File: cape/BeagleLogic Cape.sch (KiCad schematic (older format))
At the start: 21 parts, among them P1 CONN_02X14, Q1 BSS138, U1 bbb, U2 74LVCH16245, U3 AT24CS64-SSHM

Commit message: update schema, pcb to kicad5 libs
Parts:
- removed P1: CONN_02X14, Pin_Headers:Pin_Header_Angled_2x14, symbol CONN_02X14
- removed Q1: BSS138, SMD_Packages:SOT-23, symbol BSS138
- removed U3: AT24CS64-SSHM, SMD_Packages:SOIC-8-W, symbol AT24CS64-SSHM
- added J101: Conn_02x14_Odd_Even, Pin_Headers:Pin_Header_Angled_2x14, symbol Connector_Generic:Conn_02x14_Odd_Even
- added Q101: BSS138, Housings_SOT-23_SOT-143_TSOT-6:SOT-23_Handsoldering, symbol Transistor_FET:BSS138
- added U101: AT24CS64-SSHM, SMD_Packages:SOIC-8-N, symbol Memory_EEPROM:AT24CS64-SSHM
- C1, C2: symbol C -> pspice:C
- R1, R10, R12, R13, R14, R15, R2, R3, R4, R5, R6, R7, R8, R9: symbol R -> pspice:R
- U1: symbol bbb -> bbb:bbb
- U2: symbol 74LVCH16245 -> 74LVCH16245:74LVCH16245
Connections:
- wire segments 151 -> 199
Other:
- moved on the sheet: C1, C2, R1, R10, R12, R13, R14, R15, R2, R3, R4, R5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

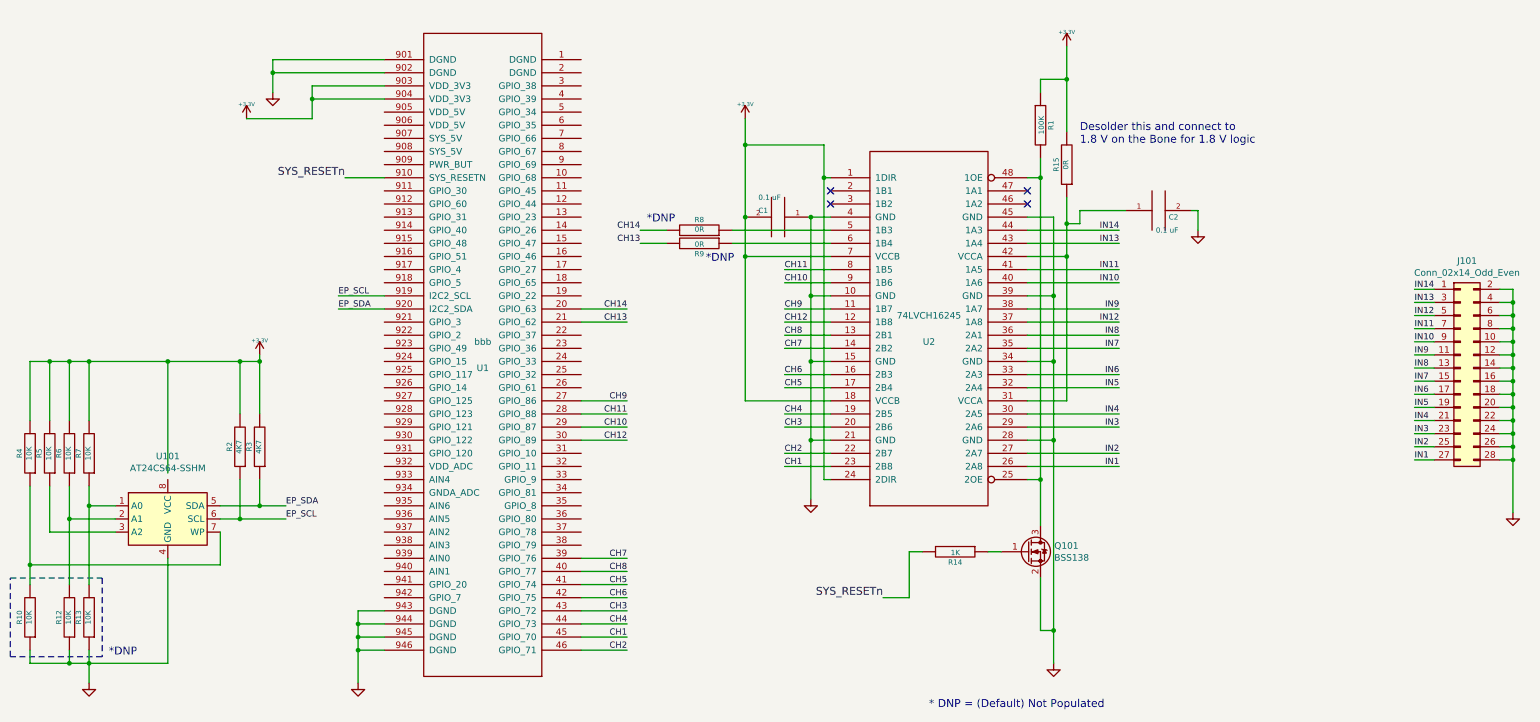
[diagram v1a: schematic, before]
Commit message: make the cape pass electrical rules check
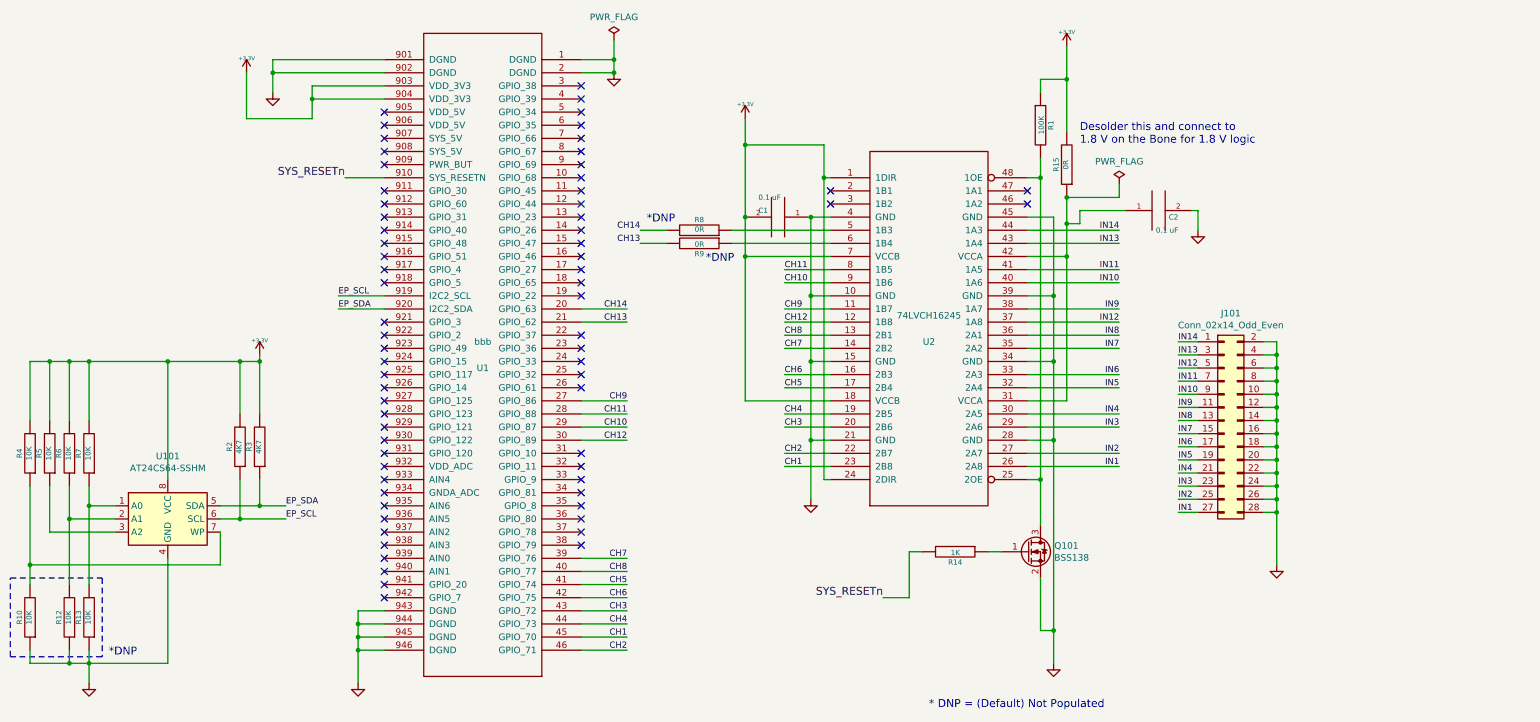
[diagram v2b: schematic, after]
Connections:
- net +3V3: now also U101.8 (VCC)
- net GND: now also U1.1 (DGND), U1.2 (DGND)
- no-connect marks 4 -> 69
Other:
- moved on the sheet: J101
